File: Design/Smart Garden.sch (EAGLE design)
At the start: 88 parts, among them IC2 MP1584EN-LF-Z, J2 POWER_JACK, T1 MMBT2222A, T3 MMBT2222A, T5 MMBT2222A, T7 MMBT2222A, U1 ESP-32S, U3 LM2596S, U4 DB107S

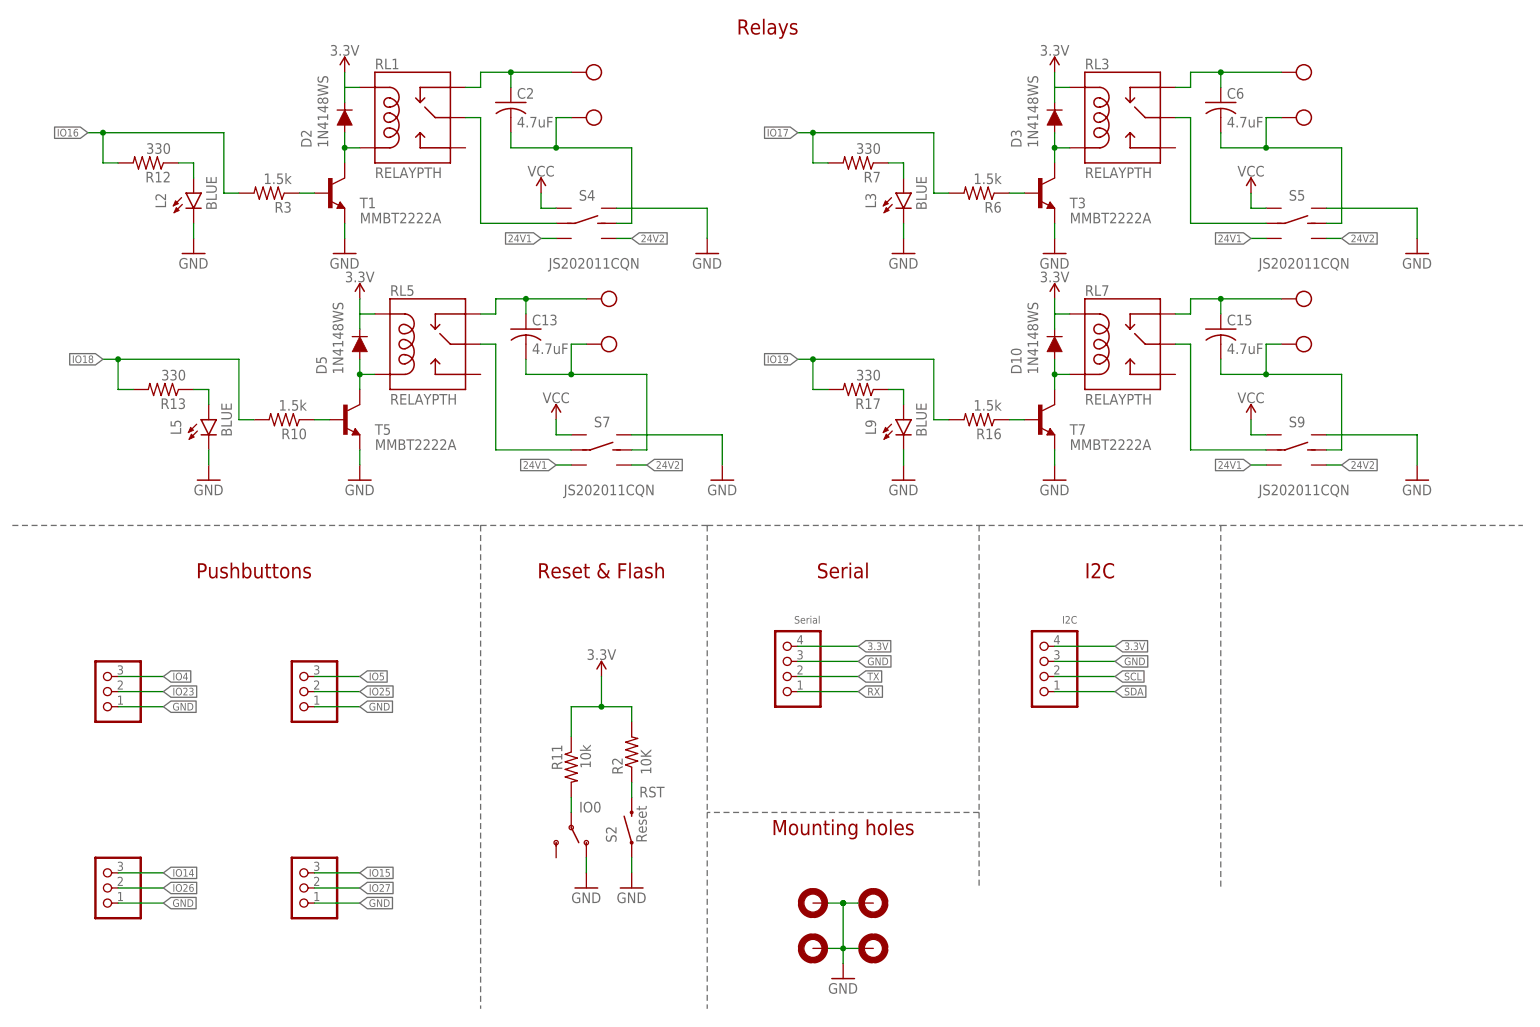
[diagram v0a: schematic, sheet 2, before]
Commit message: First commit to the CP2102 branch with schematic and a first layout of the CP2102
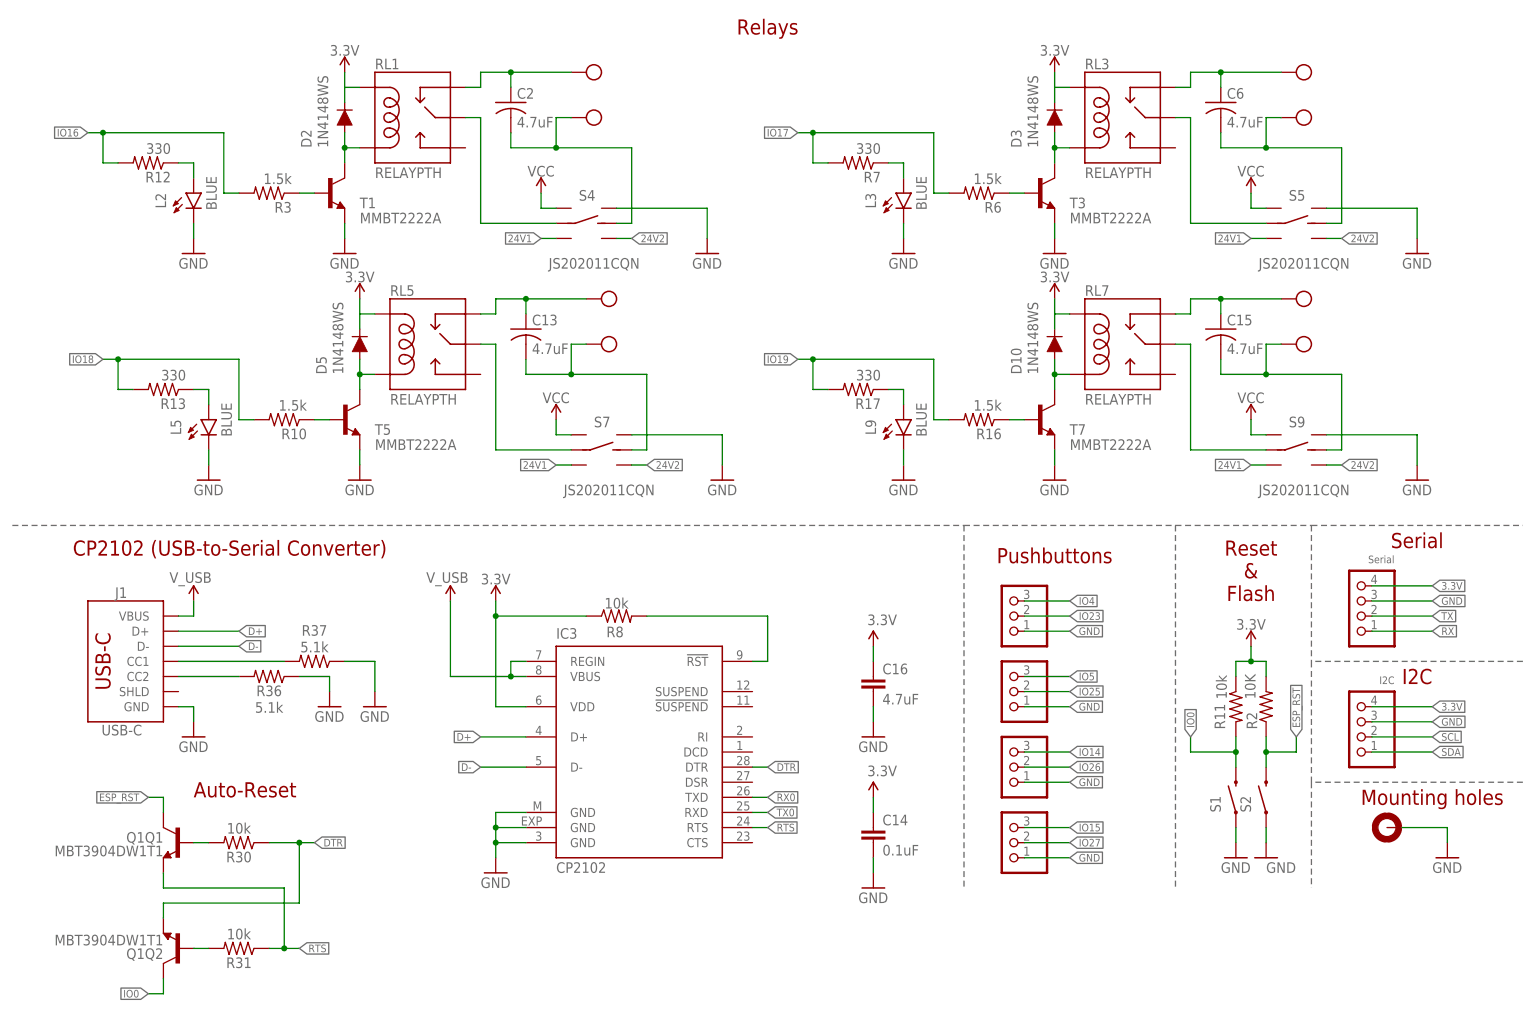
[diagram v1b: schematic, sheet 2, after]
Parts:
- removed H2, H3, H4: MOUNT-PAD-ROUND, SpaceDIY_connectors:MOUNT-PAD-ROUND
- added C14: 0.1uF, SparkFun-Capacitors:0.1UF-0402T-16V-10%
- added C16: 4.7uF, SparkFun-Capacitors:4.7UF-0402_TIGHT-6.3V-20%-X5R
- added IC3: CP2102, silabs:CP2102
- added J1: USB-C, SparkFun-Connectors:USB_C_4-LAYER-ISOLATED
- added Q1: MBT3904DW1T1, SparkFun-DiscreteSemi:TRANS_NPN_DUAL-MBT3904DW1T1
- added R30, R31, R8: 10k, SparkFun-Resistors:10KOHM-0402T-1/16W-1%
- added R36, R37: 5.1k, SparkFun-Resistors:5.1KOHM-0402T-1/16W-1%
- H1: value MOUNT-PAD-ROUND -> 92X84; device SpaceDIY_connectors:MOUNT-PAD-ROUND -> SpaceDIY_symbols:92X84
- S1: value SWITCH_SPDT -> Reset; device SparkFun-Retired:SWITCH_SPDT -> Testing:SWITCH-MOMENTARY-2SMD-4
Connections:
- removed net RST: R2.1, S2.2, U1.EN
- new net CC3: J1.CC2, R36.2
- new net CC4: J1.CC1, R37.2
- new net D+: IC3.D+, J1.D+
- new net D-: IC3.D-, J1.D-
- new net DTR: IC3.DTR, Q1Q2.E, R30.1
- new net ESP_RST: Q1Q1.C, R2.1, S2.2, U1.EN
- new net N$21: Q1Q1.B, R30.2
- new net N$22: Q1Q2.B, R31.2
- new net N$4: IC3.!RST, R8.2
- new net N$5: IC3.REGIN, IC3.VBUS
- new net RTS: IC3.RTS, Q1Q1.E, R31.1
- new net RX0: IC3.TXD
- new net TX0: IC3.RXD
- new net V_USB: J1.VBUS
- net 3.3V: now also C14.1, C16.1, IC3.VDD, R8.1
- net GND: now also C14.2, C16.2, IC3.GND, IC3.GND@EXP, IC3.GND@M, J1.GND, R36.1, R37.1, S1.1; no longer H2.MOUNT, H3.MOUNT, H4.MOUNT, S1.O
- net IO0: now also Q1Q2.C, S1.2; no longer S1.P
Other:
- note added: "Auto-Reset"
- note added: "CP2102 (USB-to-Serial Converter)"
- moved on the sheet: R11, R2, S2

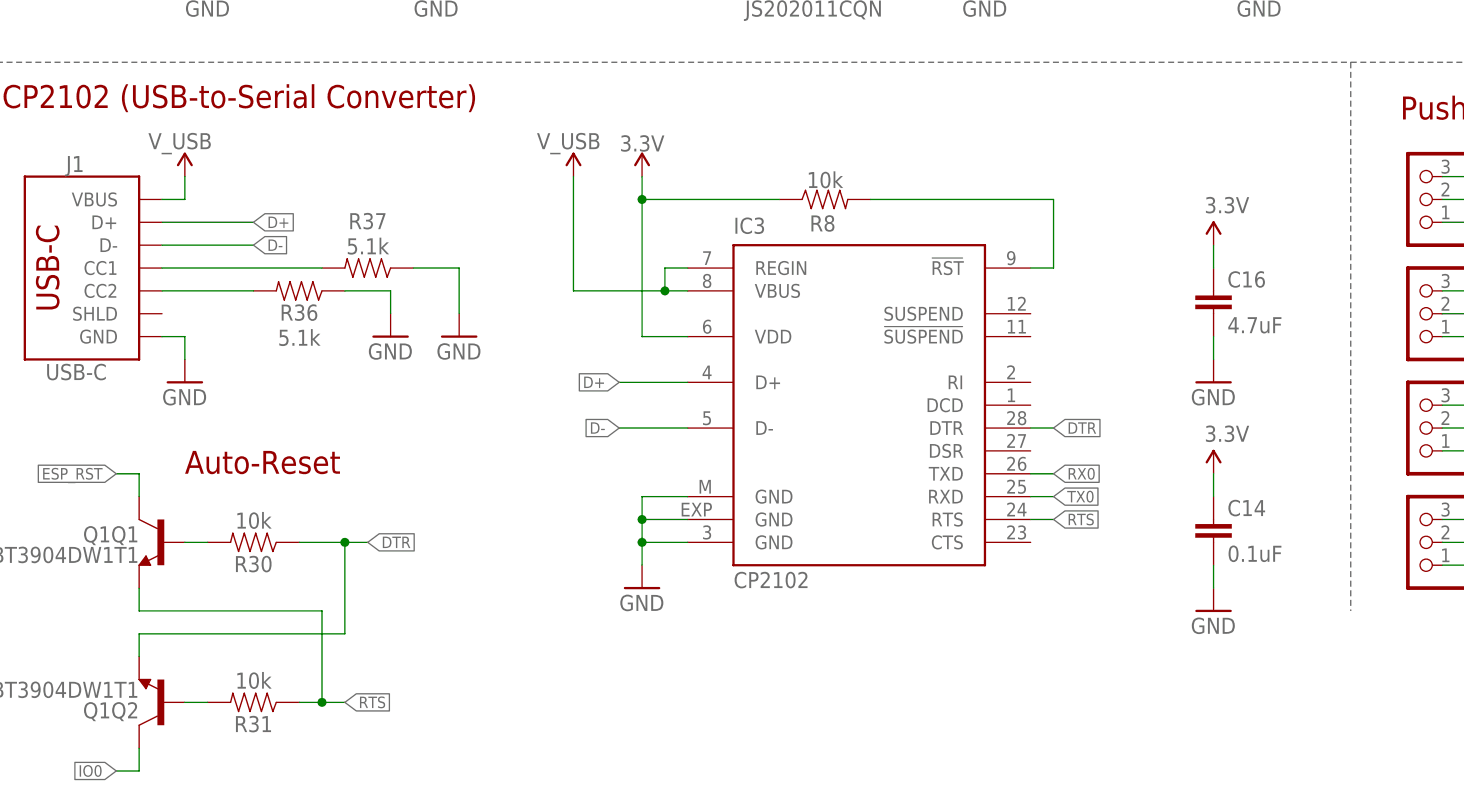
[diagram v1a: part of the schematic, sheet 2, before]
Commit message: First commit to the CP2102 branch
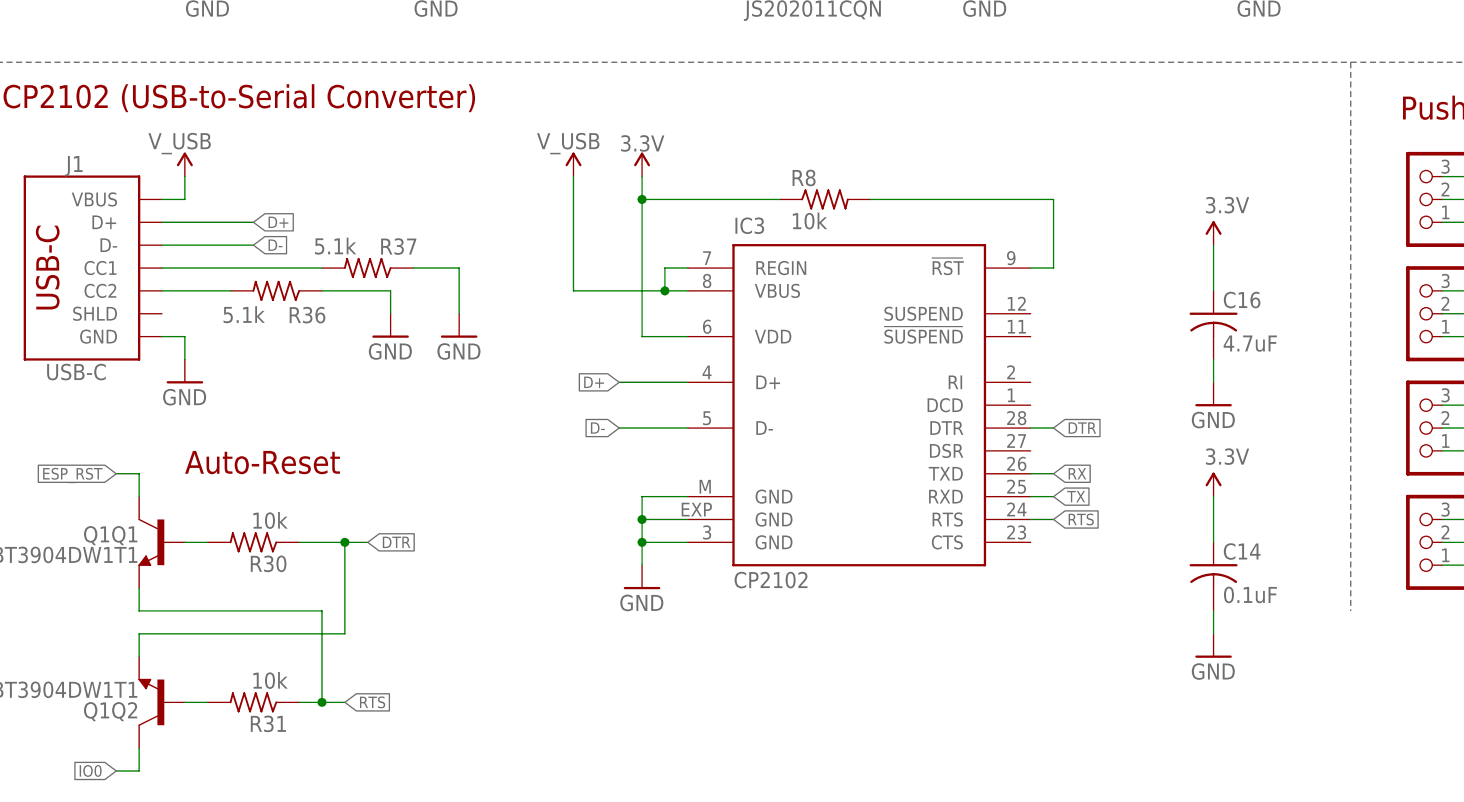
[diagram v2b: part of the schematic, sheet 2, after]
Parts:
- C1: value 330µ/50V -> 220µ/35V Low ESR; device rcl:CPOL-USG -> rcl:CPOL-USF; MFN EEVFK1H221P -> EINTRAGEN!
- C14: device SparkFun-Capacitors:0.1UF-0402T-16V-10% -> rcl:C-USC0603
- C16: device SparkFun-Capacitors:4.7UF-0402_TIGHT-6.3V-20%-X5R -> rcl:C-USC0603
- R30, R31, R8: device SparkFun-Resistors:10KOHM-0402T-1/16W-1% -> rcl:R-US_R0603
- R36, R37: device SparkFun-Resistors:5.1KOHM-0402T-1/16W-1% -> rcl:R-US_R0603
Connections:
- removed net N$5: IC3.REGIN, IC3.VBUS
- removed net RX0: IC3.TXD
- removed net TX0: IC3.RXD
- net RX: now also IC3.TXD
- net TX: now also IC3.RXD
- net V_USB: now also IC3.REGIN, IC3.VBUS
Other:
- moved on the sheet: C14, C16

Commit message: Updated design files
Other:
- moved on the sheet: C14, C16, IC3, R8

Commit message: Updated design files
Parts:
- removed Q1: MBT3904DW1T1, SparkFun-DiscreteSemi:TRANS_NPN_DUAL-MBT3904DW1T1
- added T2: MMBT3904, transistor-neu-to92:BC808-NPN-SOT23-BEC
- added T4: MMBT2222A, transistor:BC847
- D8: value SS34 -> 3A/40V/500mV; device diode:SCHOTTKY-DIODESMD -> SparkFun-DiscreteSemi:DIODE-SCHOTTKY-B340A
- D9: value RS1G -> US1M
- R23: value 40.2k -> 39k
- R24: value 124k -> 120k
- R26: value 24.9k -> 24k
- R27: value 68.1k -> 68k
- S1, S2: device Testing:SWITCH-MOMENTARY-2SMD-4 -> SpaceDIY_electromechanical:MOMENTARY-SWITCH-SPST-SMD-5.2MM-TALL
- T1: value MMBT2222A -> MMBT3904; device transistor:BC847 -> transistor-neu-to92:BC808-NPN-SOT23-BEC; LCSC C8512 -> (none)
- renumbered T7 to T6
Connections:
- net DTR: now also T1.E; no longer Q1Q2.E
- net ESP_RST: now also T2.C; no longer Q1Q1.C
- net GND: now also T4.E; no longer T1.E
- net IO0: now also T1.C; no longer Q1Q2.C
- net N$12: now also T4.C; no longer T3.C
- net N$13: now also T4.B; no longer T3.B
- net N$21: now also T2.B; no longer Q1Q1.B
- net N$22: now also T1.B; no longer Q1Q2.B
- net N$7: now also T3.C; no longer T1.C
- net N$9: now also T3.B; no longer T1.B
- net RTS: now also T2.E; no longer Q1Q1.E
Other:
- moved on the sheet: T1, T3

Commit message: Added V2R1 design files
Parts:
- removed C14: 0.1uF, rcl:C-USC0603
- removed C16: 4.7uF, rcl:C-USC0603
- removed C7: 100nF, rcl:C-USC0603
- removed D8: 3A/40V/500mV, SparkFun-DiscreteSemi:DIODE-SCHOTTKY-B340A
- removed D9: US1M, diode:DIODE-DO214AC
- removed JP1: Serial, SpaceDIY_connectors:PINHD-1X4
- removed JP6: I2C, SpaceDIY_connectors:PINHD-1X4
- removed L6: SLF10145T-100M2R5-H, SamacSys_Parts:SLF10145T-100M2R5-H
- removed L7: 47µH, Wurth_Elektronik_Passive_rev15b:WE-PD_1260/1245/1280/1210
- removed PAD1, PAD2, PAD3, PAD4: (no value), wirepad:2,54/1,1
- removed R1: (no value), pot:TRIM_US-RJ9W
- removed R11, R30, R31, R4, R8: 10k, rcl:R-US_R0603
- removed R19: 470R, rcl:R-US_R1206
- removed R2: 10K, rcl:R-US_R0603
- removed S1, S2: Reset, SpaceDIY_electromechanical:MOMENTARY-SWITCH-SPST-SMD-5.2MM-TALL
- removed T1, T2: MMBT3904, transistor-neu-to92:BC808-NPN-SOT23-BEC
- removed TP1, TP2, TP3, TP4: TPTP20SQ, testpad:TPTP20SQ
- removed U1: ESP-32S, esp32:ESP-32S
- removed U3: LM2596S, national-semiconductor:LM2596S
- added C12: 10uF, rcl:C-USC0603
- added C20: 22uF, SpaceDIY_passive_components:C0603
- added C21: 10uF, SpaceDIY_passive_components:C0603
- added C22: 100nF, SpaceDIY_passive_components:C0603
- added C23: 150pF, SpaceDIY_passive_components:C0603
- added C3: 0.1uF, rcl:C-USC0603
- added D4: 3A/40V/500mV, SparkFun-DiscreteSemi:DIODE-SCHOTTKY-B340A
- added IC1: ESP32-S2-MINI-1-N4R2, SpaceDIY_modules:ESP32-S2-MINI-1-N4R2
- added IC5: MP1584EN-LF-Z, SamacSys_Parts:MP1584EN-LF-Z
- added J7, J9: (no value), SparkFun-Connectors:CONN_04PTH
- added JP7: JUMPER-SMT_2_NC_PASTE_NO-SILK, SparkFun-Jumpers:JUMPER-SMT_2_NC_PASTE_NO-SILK
- added L1: CDRH104RNP-100NC, SpaceDIY_passive_components:CDRH104RNP-100NC
- added L4: CDRH104RNP-220NC, SpaceDIY_passive_components:CDRH104RNP-220NC
- added R20: 39k, SpaceDIY_passive_components:R0603
- added R21: 560k, SpaceDIY_passive_components:R0603
- added R29: 200k, SpaceDIY_passive_components:R0603
- added R32: 24.9k, SpaceDIY_passive_components:R0603
- added R33: 147k, SpaceDIY_passive_components:R0603
- added R34: 100k, SpaceDIY_passive_components:R0603
- added S3: Reset, SpaceDIY_electromechanical:MOMENTARY-SWITCH-SPST-SMD-5.2MM-TALL
- added S6: Flash, SpaceDIY_electromechanical:MOMENTARY-SWITCH-SPST-SMD-5.2MM-TALL
- C4: value 330µ/50V -> 10uF; device rcl:CPOL-USG -> rcl:C-USC0603; MF Panasonic -> (none); MFN EEVFK1H221P -> (none)
- C5: value 220µ/35V Low ESR -> 10uF; device rcl:CPOL-USF -> rcl:C-USC0603; MF Panasonic -> (none); MFN EINTRAGEN! -> (none)
- IC3: value CP2102 -> AMS1117-3.3; device silabs:CP2102 -> SparkFun-IC-Power:V_REG_LD1117VXXLD1117-SMD
- R10, R16, R3, R6: value 1.5k -> 1k
- R5: value 1.2k -> 10K
- RL1, RL3, RL5, RL7: value RELAYPTH -> SRD-12VDC-SL-C
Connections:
- removed net CLK: U1.CLK
- removed net CMD: U1.CMD
- removed net DTR: IC3.DTR, R30.1, T1.E
- removed net ESP_RST: R2.1, S2.2, T2.C, U1.EN
- removed net IO12: U1.IO12
- removed net IO13: U1.IO13
- removed net IO14: JP3.3, U1.IO14
- removed net IO15: JP2.3, U1.IO15
- removed net IO16: R12.2, R3.2, U1.IO16
- removed net IO17: R6.2, R7.2, U1.IO17
- removed net IO18: R10.2, R13.2, U1.IO18
- removed net IO19: R16.2, R17.2, U1.IO19
- removed net IO2: U1.IO2
- removed net IO23: JP5.2, U1.IO23
- removed net IO25: JP4.2, U1.IO25
- removed net IO26: JP3.2, U1.IO26
- removed net IO27: JP2.2, U1.IO27
- removed net IO32: R4.1, R5.2, U1.IO32
- removed net IO33: U1.IO33
- removed net IO34: U1.IO34
- removed net IO35: U1.IO35
- removed net IO4: JP5.3, U1.IO4
- removed net IO5: JP4.3, U1.IO5
- removed net N$14: D8.C, L7.1, U3.OUT
- removed net N$18: R1.E, R19.2, U3.FB
- removed net N$21: R30.2, T2.B
- removed net N$22: R31.2, T1.B
- removed net RTS: IC3.RTS, R31.1, T2.E
- removed net SD0: U1.SD0
- removed net SD1: U1.SD1
- removed net SD2: U1.SD2
- removed net SD3: U1.SD3
- removed net SVN: U1.SVN
- removed net SVP: U1.SVP
- removed net VCC: C5.+, L7.2, PAD3.P, R1.A, R1.S, R4.2, S4.L1, S5.L1, S7.L1, S9.L1
- removed net V_USB: IC3.REGIN, IC3.VBUS, J1.VBUS
- new net 12V: C20.1, D10.C, D2.C, D3.C, D5.C, L4.2, R21.2, RL1.COIL1, RL3.COIL1, RL5.COIL1, RL7.COIL1, S4.L1, S5.L1, S7.L1, S9.L1
- new net 5V: C4.1, IC3.IN, J1.VBUS, J7.1
- new net IN_1: IC1.IO1, JP5.3
- new net IN_2: IC1.IO2, JP4.3
- new net IN_3: IC1.IO3, JP3.3
- new net IN_4: IC1.IO4, JP2.3
- new net N$25: C22.1, IC5.BST
- new net N$26: C22.2, D4.C, IC5.SW, L4.1
- new net N$41: IC5.FB, R20.1, R21.1
- new net N$42: C23.2, R33.1
- new net N$43: C23.1, IC5.COMP
- new net N$44: IC5.FREQ, R29.1
- new net N$45: IC5.EN, R32.1, R34.2
- new net OUT_1: IC1.IO5, JP5.2
- new net OUT_2: IC1.IO6, JP4.2
- new net OUT_3: IC1.IO7, JP3.2
- new net OUT_4: IC1.IO8, JP2.2
- new net RELAY_1: IC1.IO10, R12.2, R3.2
- new net RELAY_2: IC1.IO11, R6.2, R7.2
- new net RELAY_3: IC1.IO12, R10.2, R13.2
- new net RELAY_4: IC1.IO13, R16.2, R17.2
- new net RST: IC1.EN, R5.1, S3.2
- net 24V: now also C21.1, IC5.VIN, R34.1; no longer C4.+, D9.C, PAD1.P, TP1.TP, U3.VIN
- net 24V1: now also U4.AC2; no longer U4.AC1
- net 24V2: now also U4.AC1; no longer U4.AC2
- net 3.3V: now also C12.1, C3.1, C5.1, IC1.3V3, IC3.OUT, J9.2, JP7.1, L1.2, R5.2; no longer C14.1, C16.1, C7.1, D10.C, D2.C, D3.C, D5.C, IC3.VDD, JP1.4, JP6.4, L6.2, R11.1, R2.2, R22.2, R8.1, RL1.COIL1, RL3.COIL1, RL5.COIL1, RL7.COIL1, TP3.TP, U1.3V3
- net D+: now also IC1.IO20; no longer IC3.D+
- net D-: now also IC1.IO19; no longer IC3.D-
- net GND: now also C12.2, C20.2, C21.2, C3.2, C4.2, C5.2, D4.A, IC1.GND_1, IC1.GND_10, IC1.GND_11, IC1.GND_12, IC1.GND_13, IC1.GND_14, IC1.GND_15, IC1.GND_16, IC1.GND_17, IC1.GND_18, IC1.GND_19, IC1.GND_2, IC1.GND_20, IC1.GND_21, IC1.GND_22, IC1.GND_23, IC1.GND_24, IC1.GND_25, IC1.GND_26, IC1.GND_27, IC1.GND_28, IC1.GND_29, IC1.GND_3, IC1.GND_30, IC1.GND_31, IC1.GND_32, IC1.GND_33, IC1.GND_4, IC1.GND_5, IC1.GND_6, IC1.GND_7, IC1.GND_8, IC1.GND_9, IC5.EP, IC5.GND, J7.2, J9.1, R20.2, R29.2, R32.2, R33.2, S3.1, S6.1; no longer C14.2, C16.2, C4.-, C5.-, C7.2, D8.A, D9.A, IC3.GND@EXP, IC3.GND@M, JP1.3, JP6.3, PAD2.P, PAD4.P, R19.1, R5.1, S1.1, S2.1, TP2.TP, TP4.TP, U1.GND@1, U1.GND@2, U1.GND@3, U1.GND@4, U3.!ON!/OFF, U3.GND
- net IO0: now also IC1.IO0, S6.2; no longer R11.2, S1.2, T1.C, U1.IO0
- net N$35: now also L1.1; no longer L6.1
- net N$4: now also JP7.2, R22.2; no longer IC3.!RST, R8.2
- net RX: now also IC1.RXD0, J7.4; no longer IC3.TXD, JP1.1, U1.U0RXD
- net SCL: now also IC1.IO34, J9.4; no longer JP6.2, U1.IO22
- net SDA: now also IC1.IO33, J9.3; no longer JP6.1, U1.IO21
- net TX: now also IC1.TXD0, J7.3; no longer IC3.RXD, JP1.2, U1.U0TXD
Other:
- note added: "12V Power supply"
- note added: "3.3V Power supply"
- note added: "IIC port"
- note added: "Pin heads"
- note added: "Reset & Flash switches"
- note added: "Serial port"
- note added: "USB-C"
- note removed: "3.3V Power source"
- note removed: "Auto-Reset"
- note removed: "CP2102 (USB-to-Serial Converter)"
- note removed: "Flash"
- note removed: "I2C"
- note removed: "Mounting holes"
- note removed: "Out 1"
- note removed: "Out 2"
- note removed: "Out 3"
- note removed: "Out 4"
- note removed: "PB_In_1"
- note removed: "PB_In_2"
- note removed: "PB_In_3"
- note removed: "PB_In_4"
- note removed: "PB_LED_1"
- note removed: "PB_LED_2"
- note removed: "PB_LED_3"
- note removed: "PB_LED_4"
- note removed: "Pushbuttons"
- note removed: "RST"
- note removed: "Reset & Flash"
- note removed: "SCL"
- note removed: "SDA"
- note removed: "Serial"
- note removed: "VCC Regulable power source"
- note removed: "VCC_ADC"
